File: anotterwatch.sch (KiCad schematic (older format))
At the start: 51 parts, among them J3 Micro_SD_Card, Q1 AO3400, Q2 AO3400, Q3 npn, Q4 npn, Q7 AO3400, U1 TP4056, U12 BMI270, U2 ESP32, U3 CH340C, U4 ST7789V

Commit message: Schematic cleanup
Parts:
- removed C2, C3: 100n, Capacitor_SMD:C_0603_1608Metric, symbol Device:C_Small
- removed R36: 2k5, Resistor_SMD:R_0603_1608Metric, symbol Device:R_Small
- removed R43: 47k, Resistor_SMD:R_0603_1608Metric, symbol Device:R_Small
- removed U1: TP4056, symbol badgelib:TP4056
- added C?: 100n, Capacitor_SMD:C_0603_1608Metric, symbol Device:C_Small
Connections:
- net GND: now also C?.2
- net VBUS: now also C?.1
- net CH340_V3: no longer names the net of C4.1, U3.4 (V3)
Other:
- moved on the sheet: C4, D1, D2, D3, D4, D5, D6, J3, Q1, Q3, Q4, Q7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

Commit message: added datasheets and descriptions
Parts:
- U12: Field4 (none) -> There is no BMI270 datasheet released yet
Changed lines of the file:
@@
 F 1 "AO3400" H 10855 5855 50  0000 L CNN
 F 2 "Package_TO_SOT_SMD:SOT-23" H 10850 6000 50  0001 C CNN
-F 3 "~" H 10650 5900 50  0001 C CNN
+F 3 "http://aosmd.com/pdfs/datasheet/AO3400.pdf" H 10650 5900 50  0001 C CNN
 	1    10650 5900
 	1    0    0    -1
@@
 F 1 "BMI270" H 1800 7350 50  0000 C CNN
 F 2 "badgelib:BMI270" H 1500 7550 50  0001 C CNN
-F 3 "" H 1500 7550 50  0001 C CNN
+F 3 "http://www.mouser.com/ds/2/783/BST-BMI160-DS000-07-786474.pdf" H 1500 7550 50  0001 C CNN
+F 4 "There is no BMI270 datasheet released yet" H 1550 6900 50  0001 C CNN "Field4"
 	1    1550 6900
 	1    0    0    -1
@@
 F 1 "AO3400" H 9405 2855 50  0000 L CNN
 F 2 "Package_TO_SOT_SMD:SOT-23" H 9400 3000 50  0001 C CNN
-F 3 "~" H 9200 2900 50  0001 C CNN
+F 3 "http://aosmd.com/pdfs/datasheet/AO3400.pdf" H 9200 2900 50  0001 C CNN
 	1    9200 2900
 	1    0    0    -1

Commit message: add anotation
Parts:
- R30, R32, R35: footprint (none) -> Resistor_SMD:R_0603_1608Metric
- gave numbers to parts that had none: 1
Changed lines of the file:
@@
 F 0 "R30" V 4150 6850 50  0000 C CNN
 F 1 "10" V 4350 6850 50  0000 C CNN
-F 2 "" H 4250 6850 50  0001 C CNN
+F 2 "Resistor_SMD:R_0603_1608Metric" H 4250 6850 50  0001 C CNN
 F 3 "~" H 4250 6850 50  0001 C CNN
 	1    4250 6850
@@
 F 0 "R32" V 4300 7000 50  0000 C CNN
 F 1 "220" V 4500 7000 50  0000 C CNN
-F 2 "" H 4400 7000 50  0001 C CNN
+F 2 "Resistor_SMD:R_0603_1608Metric" H 4400 7000 50  0001 C CNN
 F 3 "~" H 4400 7000 50  0001 C CNN
 	1    4400 7000
@@
 F 0 "R35" V 5800 2750 50  0000 C CNN
 F 1 "10" V 6000 2750 50  0000 C CNN
-F 2 "" H 5900 2750 50  0001 C CNN
+F 2 "Resistor_SMD:R_0603_1608Metric" H 5900 2750 50  0001 C CNN
 F 3 "~" H 5900 2750 50  0001 C CNN
 	1    5900 2750
@@
 	1850 2650 1850 2750
 $Comp
-L Device:C_Small C?
+L Device:C_Small C30
 U 1 1 5C7CD696
 P 950 2650
-F 0 "C?" H 1042 2696 50  0000 L CNN
+F 0 "C30" H 1042 2696 50  0000 L CNN
 F 1 "100n" H 1042 2605 50  0000 L CNN
 F 2 "Capacitor_SMD:C_0603_1608Metric" H 950 2650 50  0001 C CNN
@@
 $EndComp
 $Comp
-L power:GND #PWR?
+L power:GND #PWR0144
 U 1 1 5C7CD69D
 P 950 2800
-F 0 "#PWR?" H 950 2550 50  0001 C CNN
+F 0 "#PWR0144" H 950 2550 50  0001 C CNN
 F 1 "GND" H 955 2627 50  0000 C CNN
 F 2 "" H 950 2800 50  0001 C CNN

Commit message: added SD Card socket footprint
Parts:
- J3: footprint (none) -> ST-TF-003A:SUNTECH_ST-TF-003A
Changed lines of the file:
@@
 F 0 "J3" H 5600 7467 50  0000 C CNN
 F 1 "Micro_SD_Card" H 5600 7376 50  0000 C CNN
-F 2 "" H 6800 7050 50  0001 C CNN
+F 2 "ST-TF-003A:SUNTECH_ST-TF-003A" H 6800 7050 50  0001 C CNN
 F 3 "http://katalog.we-online.de/em/datasheet/693072010801.pdf" H 5650 6750 50  0001 C CNN
 	1    5650 6750

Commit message: added shitty addon todo
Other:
- note added: "Todo add shitty addon connector\n"
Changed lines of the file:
@@
 Wire Wire Line
 	950  2500 950  2450
+Text Notes 9550 4250 0    50   ~ 0
+Todo add shitty addon connector\n
 $EndSCHEMATC

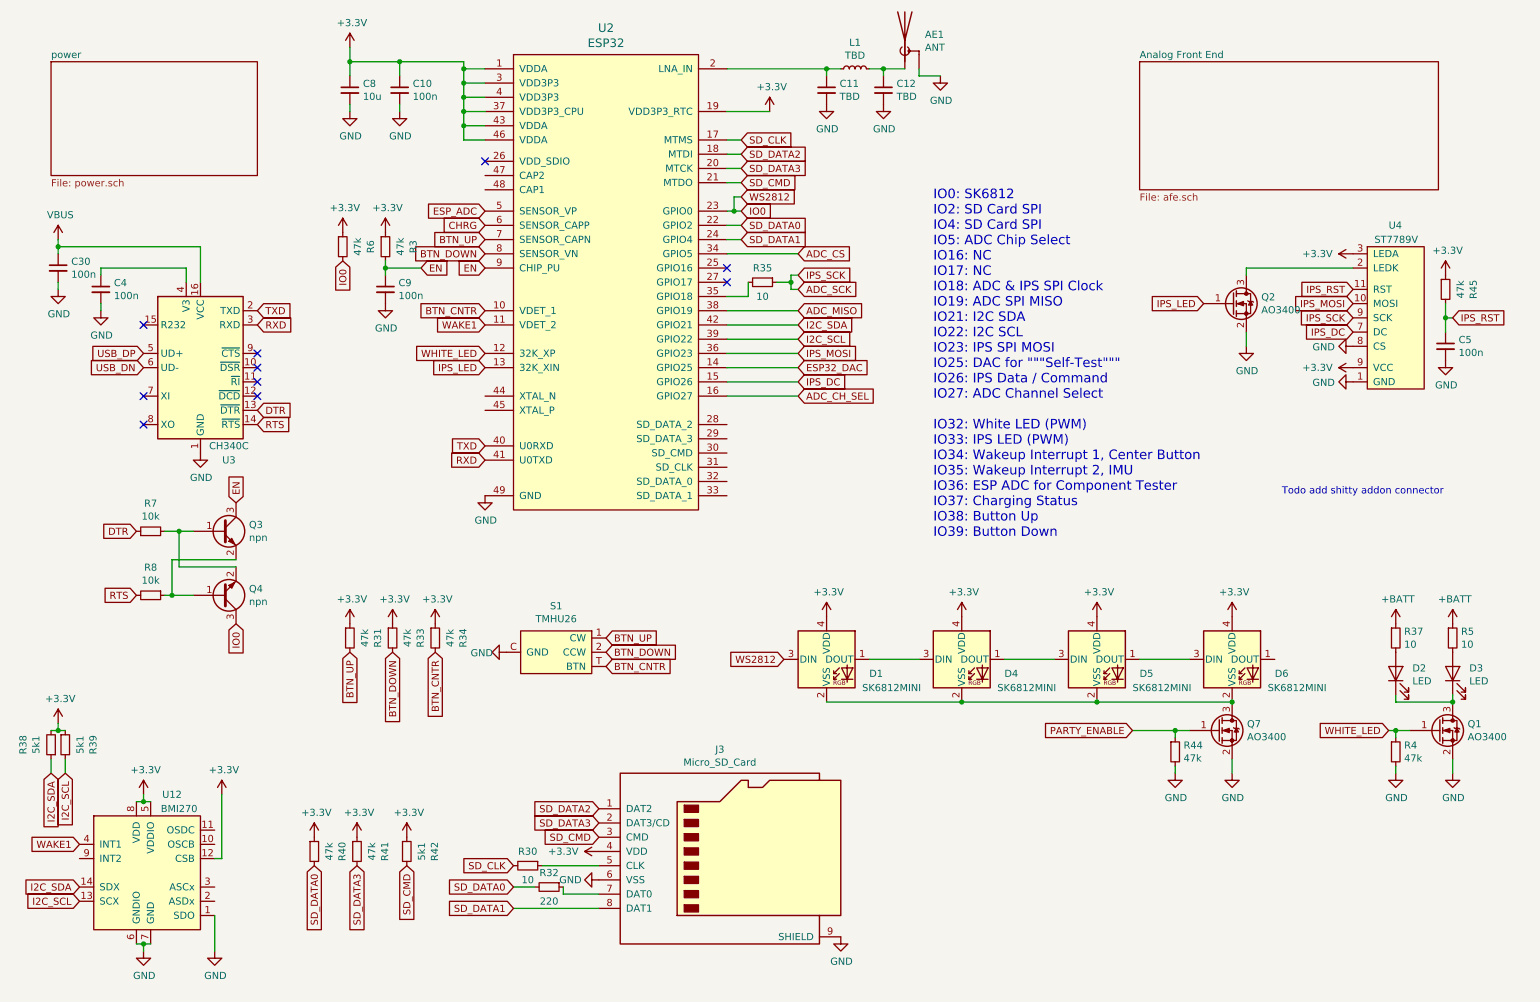
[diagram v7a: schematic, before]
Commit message: UPD: finalized schematic, started layout
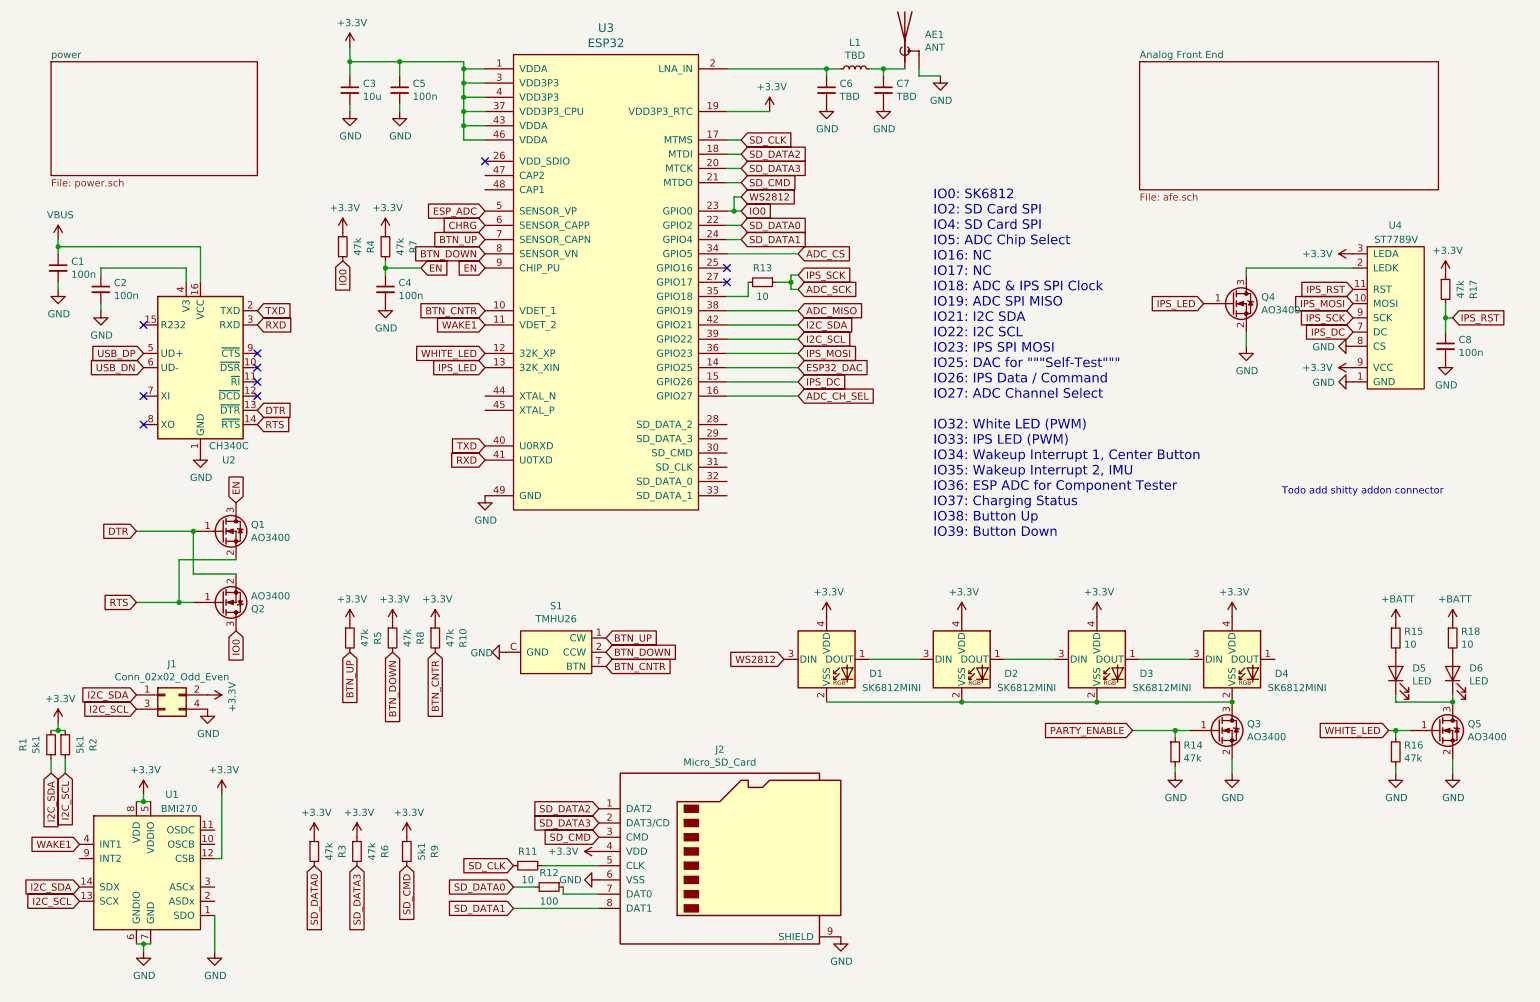
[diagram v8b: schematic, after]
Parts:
- removed Q3, Q4: npn, Package_TO_SOT_SMD:SOT-23, symbol Device:Q_NPN_BEC
- removed R7, R8: 10k, Resistor_SMD:R_0603_1608Metric, symbol Device:R_Small
- added J1: Conn_02x02_Odd_Even, Connector_PinSocket_2.54mm:PinSocket_2x02_P2.54mm_Vertical_SMD, symbol Connector_Generic:Conn_02x02_Odd_Even
- added Q1, Q2: AO3400, Package_TO_SOT_SMD:SOT-23, symbol Device:Q_NMOS_GSD
- R12: renamed from R32; value 220 -> 100
- renumbered C30 to C1, C4 to C2, C8 to C3, C9 to C4, C10 to C5, C11 to C6, C12 to C7, C5 to C8, D4 to D2, D5 to D3, D6 to D4, D2 to D5, D3 to D6, J3 to J2, Q7 to Q3, Q2 to Q4, Q1 to Q5, R38 to R1, R34 to R10, R30 to R11, R35 to R13, R44 to R14, R37 to R15, R4 to R16, R45 to R17, R5 to R18, R39 to R2, R40 to R3, R6 to R4, R31 to R5, R41 to R6, R3 to R7, R33 to R8, R42 to R9, U12 to U1, U3 to U2, U2 to U3
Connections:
- net +3V3: now also J1.2 (Pin_2)
- net DTR: now also Q1.1 (G), Q2.2 (S)
- net EN: now also Q1.3 (D)
- net GND: now also J1.4 (Pin_4)
- net I2C_SCL: now also J1.3 (Pin_3)
- net I2C_SDA: now also J1.1 (Pin_1)
- net IO0: now also Q2.3 (D)
- net RTS: now also Q1.2 (S), Q2.1 (G)
